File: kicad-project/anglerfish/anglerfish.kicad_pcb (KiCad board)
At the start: 2 copper layers, 276.9 x 188 mm, 4 parts

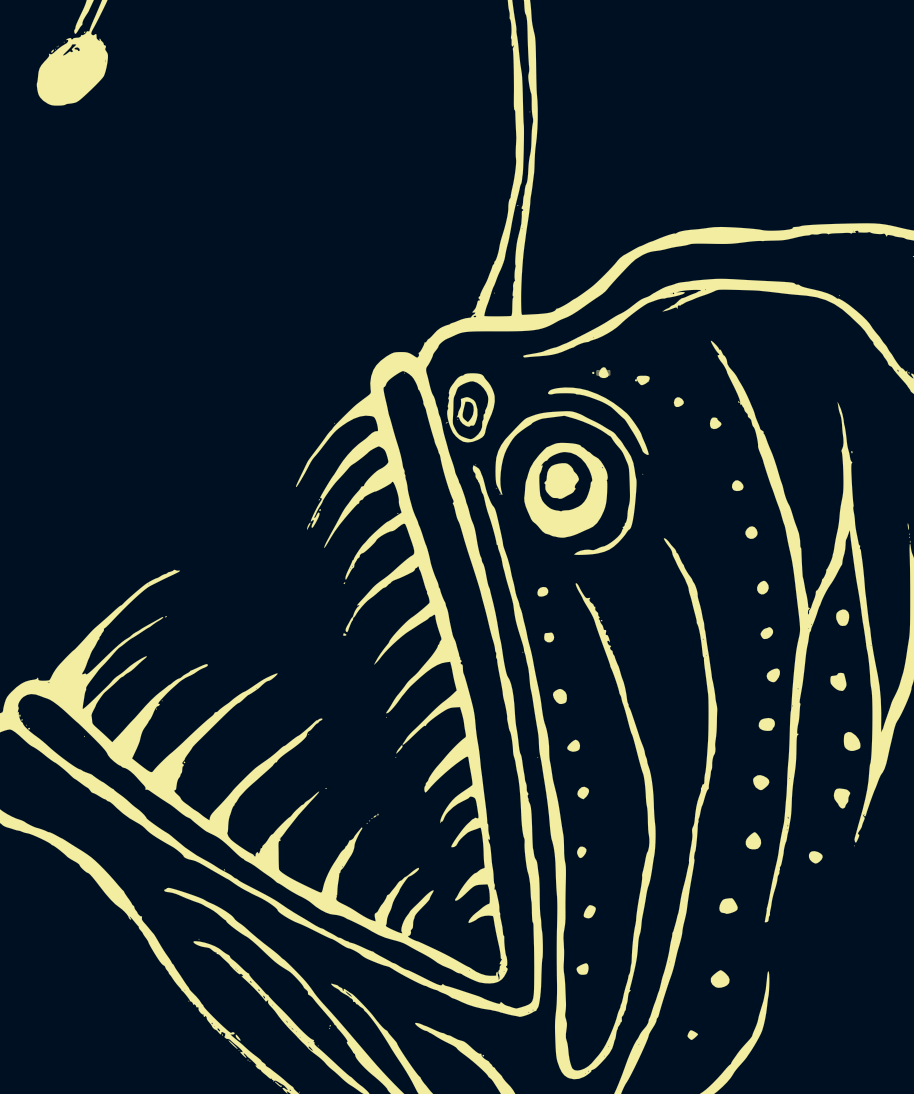
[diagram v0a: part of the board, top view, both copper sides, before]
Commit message: Added the 0402 whites. Also added the APA.
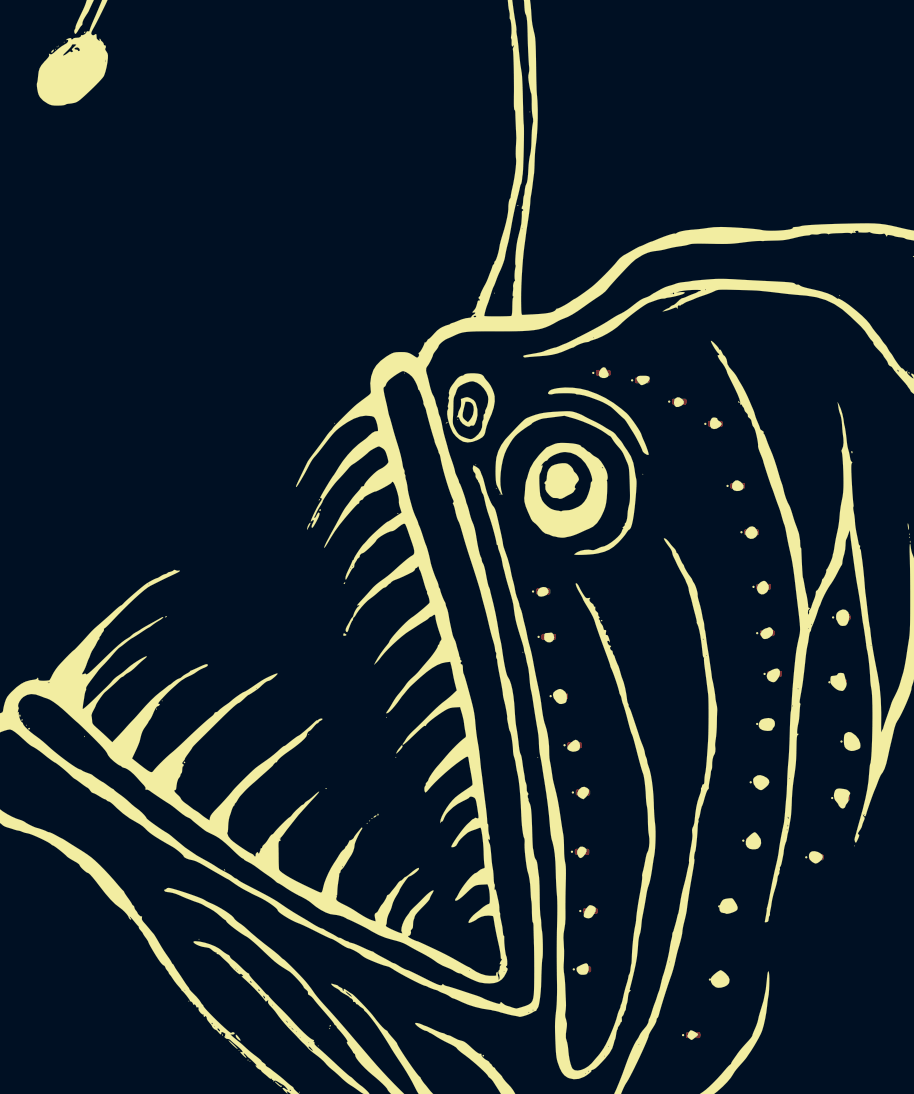
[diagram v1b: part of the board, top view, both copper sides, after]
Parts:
- added D10: LED, LED_SMD:LED_0402_1005Metric, F.Cu at (135.6, 120.1)
- added D11: LED, LED_SMD:LED_0402_1005Metric, F.Cu at (134.8, 125.5)
- added D12: LED, LED_SMD:LED_0402_1005Metric, F.Cu at (134.1, 131.8)
- added D13: LED, LED_SMD:LED_0402_1005Metric, F.Cu at (133.3, 138.1)
- added D14: LED, LED_SMD:LED_0402_1005Metric, F.Cu at (130.7, 145.2)
- added D15: LED, LED_SMD:LED_0402_1005Metric, F.Cu at (129.7, 153.1)
- added D16: LED, LED_SMD:LED_0402_1005Metric, F.Cu at (126.8, 159.1)
- added D17: LED, LED_SMD:LED_0402_1005Metric, F.Cu at (115.0, 152.0)
- added D18: LED, LED_SMD:LED_0402_1005Metric, F.Cu at (115.7, 145.7)
- added D19: LED, LED_SMD:LED_0402_1005Metric, F.Cu at (114.8, 139.3)
- added D20: LED, LED_SMD:LED_0402_1005Metric, F.Cu at (114.9, 132.9)
- added D21: LED, LED_SMD:LED_0402_1005Metric, F.Cu at (114.0, 127.8)
- added D22: LED, LED_SMD:LED_0402_1005Metric, F.Cu at (112.5, 122.5)
- added D23: LED, LED_SMD:LED_0402_1005Metric, F.Cu at (111.2, 116.1)
- added D24: LED, LED_SMD:LED_0402_1005Metric, F.Cu at (110.6, 111.2)
- added D25: LED, LED_SMD:LED_0402_1005Metric, F.Cu at (143.0, 114.0)
- added D26: LED, LED_SMD:LED_0402_1005Metric, F.Cu at (142.6, 121.0)
- added D27: LED, LED_SMD:LED_0402_1005Metric, F.Cu at (143.9, 127.4)
- added D28: LED, LED_SMD:LED_0402_1005Metric, F.Cu at (142.9, 133.5)
- added D29: LED, LED_SMD:LED_0402_1005Metric, F.Cu at (140.1, 139.9)
- added D4: LED, LED_SMD:LED_0402_1005Metric, F.Cu at (125.3, 90.7)
- added D5: LED, LED_SMD:LED_0402_1005Metric, F.Cu at (129.2, 93.1)
- added D6: LED, LED_SMD:LED_0402_1005Metric, F.Cu at (131.6, 99.8)
- added D7: LED, LED_SMD:LED_0402_1005Metric, F.Cu at (133.1, 104.8)
- added D8: LED, LED_SMD:LED_0402_1005Metric, F.Cu at (134.4, 110.7)
- added D9: LED, LED_SMD:LED_0402_1005Metric, F.Cu at (134.8, 115.7)
- D1: value LED -> APA102-2020; footprint LED_SMD:LED_0603_1608Metric -> LED_SMD:LED-APA102-2020
- D3: footprint LED_SMD:LED_0201_0603Metric -> LED_SMD:LED_0402_1005Metric
- moved D1 0.67 mm to (59.8, 55.2)
- moved D3 0.20 mm to (121.3, 88.4)

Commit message: Added the photodiode.
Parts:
- added C1: 100n, Capacitor_SMD:C_0402_1005Metric, B.Cu at (106.2, 91.6)
- added D30: LED, LED_SMD:LED_0402_1005Metric, F.Cu at (112.5, 99.3)
- added TP1: TestPoint, TestPoint:TestPoint_Pad_D1.5mm, B.Cu at (99.5, 91.7)
- added TP2: TestPoint, TestPoint:TestPoint_Pad_D1.5mm, B.Cu at (101.9, 88.3)
- added TP3: TestPoint, TestPoint:TestPoint_Pad_D1.5mm, B.Cu at (105.3, 94.1)
- added U1: APDS-9306-065, OptoDevice:Broadcom_DFN-6_2x2mm_P0.65mm, F.Cu at (102.6, 91.7)

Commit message: ZIF connector added.
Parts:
- added J1: Conn_01x34_MountingPin, Connector_FFC-FPC:Hirose_FH12-34S-0.5SH_1x34-1MP_P0.50mm_Horizontal, B.Cu at (151.0, 52.0)

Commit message: Schematic entered. Adding placing the resistors in the layout now.
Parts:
- added C2: 100n, Capacitor_SMD:C_0402_1005Metric, F.Cu at (60.0, 62.0)
- added R1: R_Small_US, Resistor_SMD:R_0402_1005Metric, B.Cu at (117.1, 86.4)
- added R10: R_Small_US, Resistor_SMD:R_0402_1005Metric, F.Cu at (35.1, 85.0)
- added R11: R_Small_US, Resistor_SMD:R_0402_1005Metric, B.Cu at (134.1, 130.7)
- added R12: R_Small_US, Resistor_SMD:R_0402_1005Metric, B.Cu at (133.3, 137.0)
- added R13: R_Small_US, Resistor_SMD:R_0402_1005Metric, F.Cu at (38.6, 83.0)
- added R14: R_Small_US, Resistor_SMD:R_0402_1005Metric, F.Cu at (41.5, 81.0)
- added R15: R_Small_US, Resistor_SMD:R_0402_1005Metric, F.Cu at (35.7, 83.0)
- added R16: R_Small_US, Resistor_SMD:R_0402_1005Metric, F.Cu at (38.0, 87.0)
- added R17: R_Small_US, Resistor_SMD:R_0402_1005Metric, F.Cu at (40.9, 85.0)
- added R18: R_Small_US, Resistor_SMD:R_0402_1005Metric, B.Cu at (114.8, 138.2)
- added R19: R_Small_US, Resistor_SMD:R_0402_1005Metric, B.Cu at (114.9, 131.8)
- added R2: R_Small_US, Resistor_SMD:R_0402_1005Metric, F.Cu at (28.6, 88.1)
- added R20: R_Small_US, Resistor_SMD:R_0402_1005Metric, F.Cu at (43.8, 87.0)
- added R21: R_Small_US, Resistor_SMD:R_0402_1005Metric, B.Cu at (112.5, 121.4)
- added R22: R_Small_US, Resistor_SMD:R_0402_1005Metric, F.Cu at (43.8, 85.0)
- added R23: R_Small_US, Resistor_SMD:R_0402_1005Metric, F.Cu at (44.5, 83.0)
- added R24: R_Small_US, Resistor_SMD:R_0402_1005Metric, B.Cu at (143.0, 112.7)
- added R25: R_Small_US, Resistor_SMD:R_0402_1005Metric, F.Cu at (40.9, 87.0)
- added R26: R_Small_US, Resistor_SMD:R_0402_1005Metric, B.Cu at (143.9, 126.3)
- added R27: R_Small_US, Resistor_SMD:R_0402_1005Metric, F.Cu at (38.0, 85.0)
- added R28: R_Small_US, Resistor_SMD:R_0402_1005Metric, F.Cu at (56.0, 71.0)
- added R29: R_Small_US, Resistor_SMD:R_0402_1005Metric, F.Cu at (41.5, 83.0)
- added R3: R_Small_US, Resistor_SMD:R_0402_1005Metric, F.Cu at (32.2, 84.5)
- added R4: R_Small_US, Resistor_SMD:R_0402_1005Metric, F.Cu at (35.7, 81.0)
- added R5: R_Small_US, Resistor_SMD:R_0402_1005Metric, B.Cu at (131.6, 99.8)
- added R6: R_Small_US, Resistor_SMD:R_0402_1005Metric, B.Cu at (133.1, 103.7)
- added R7: R_Small_US, Resistor_SMD:R_0402_1005Metric, F.Cu at (32.2, 86.5)
- added R8: R_Small_US, Resistor_SMD:R_0402_1005Metric, F.Cu at (38.6, 81.0)
- added R9: R_Small_US, Resistor_SMD:R_0402_1005Metric, B.Cu at (135.6, 119.0)
- added TP4: TestPoint, TestPoint:TestPoint_Pad_D1.5mm, F.Cu at (32.5, 81.8)
- added TP5: TestPoint, TestPoint:TestPoint_Pad_D1.5mm, F.Cu at (28.9, 85.3)
- added TP6: TestPoint, TestPoint:TestPoint_Pad_D1.5mm, F.Cu at (25.4, 88.9)
- added TP7: TestPoint, TestPoint:TestPoint_Pad_D1.5mm, F.Cu at (28.9, 81.8)
- added TP8: TestPoint, TestPoint:TestPoint_Pad_D1.5mm, F.Cu at (25.4, 85.3)
- added TP9: TestPoint, TestPoint:TestPoint_Pad_D1.5mm, F.Cu at (25.4, 81.8)
- J1: value Conn_01x34_MountingPin -> Hirose_FH12-34S-0.5SH_1x34
- moved D1 0.28 mm to (60.0, 55.0)
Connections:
- net /Sheet5FEEB7DF/light-int renamed /photodiode-1/photodiode-int
- net Net-(D1-Pad2) renamed /led-apa102-1/apa102-cko
- net Net-(D1-Pad3) renamed /led-apa102-1/apa102-sdo
- D1 pad 4: Net-(D1-Pad4) -> /led-apa102-1/apa102-sdi
- D1 pad 5: Net-(D1-Pad5) -> /led-apa102-1/apa102-cki
- D1 pad 6: Net-(D1-Pad6) -> GND
- D10 pad 2: Net-(D10-Pad2) -> /LED_GROUP_2
- D11 pad 2: Net-(D11-Pad2) -> /LED_GROUP_2
- D12 pad 2: Net-(D12-Pad2) -> /LED_GROUP_3
- D13 pad 2: Net-(D13-Pad2) -> /LED_GROUP_3
- D14 pad 2: Net-(D14-Pad2) -> /LED_GROUP_3
- D15 pad 2: Net-(D15-Pad2) -> /LED_GROUP_3
- D16 pad 2: Net-(D16-Pad2) -> /LED_GROUP_3
- D17 pad 2: Net-(D17-Pad2) -> /LED_GROUP_4
- D18 pad 2: Net-(D18-Pad2) -> /LED_GROUP_4
- D19 pad 2: Net-(D19-Pad2) -> /LED_GROUP_4
- D2 pad 2: Net-(D2-Pad2) -> /LED_GROUP_1
- D20 pad 2: Net-(D20-Pad2) -> /LED_GROUP_4
- D21 pad 2: Net-(D21-Pad2) -> /LED_GROUP_4
- D22 pad 2: Net-(D22-Pad2) -> /LED_GROUP_5
- D23 pad 2: Net-(D23-Pad2) -> /LED_GROUP_5
- D24 pad 2: Net-(D24-Pad2) -> /LED_GROUP_5
- D25 pad 2: Net-(D25-Pad2) -> /LED_GROUP_5
- D26 pad 2: Net-(D26-Pad2) -> /LED_GROUP_5
- D27 pad 2: Net-(D27-Pad2) -> /LED_GROUP_6
- D28 pad 2: Net-(D28-Pad2) -> /LED_GROUP_6
- D29 pad 2: Net-(D29-Pad2) -> /LED_GROUP_6
- D3 pad 2: Net-(D3-Pad2) -> /LED_GROUP_1
- D30 pad 2: Net-(D30-Pad2) -> /LED_GROUP_6
- D4 pad 2: Net-(D4-Pad2) -> /LED_GROUP_1
- D5 pad 2: Net-(D5-Pad2) -> /LED_GROUP_1
- D6 pad 2: Net-(D6-Pad2) -> /LED_GROUP_1
- D7 pad 2: Net-(D7-Pad2) -> /LED_GROUP_2
- D8 pad 2: Net-(D8-Pad2) -> /LED_GROUP_2
- D9 pad 2: Net-(D9-Pad2) -> /LED_GROUP_2
- J1 pad 1: Net-(J1-Pad1) -> +3V3
- J1 pad 11: Net-(J1-Pad11) -> /led-apa102-1/apa102-sdi
- J1 pad 12: Net-(J1-Pad12) -> /led-apa102-1/apa102-cki
- J1 pad 14: Net-(J1-Pad14) -> GND
- J1 pad 15: Net-(J1-Pad15) -> /LED_GROUP_1
- J1 pad 16: Net-(J1-Pad16) -> /LED_GROUP_2
- J1 pad 17: Net-(J1-Pad17) -> /LED_GROUP_3
- J1 pad 18: Net-(J1-Pad18) -> /LED_GROUP_4
- J1 pad 19: Net-(J1-Pad19) -> /LED_GROUP_5
- J1 pad 2: Net-(J1-Pad2) -> +3V3
- J1 pad 20: Net-(J1-Pad20) -> /LED_GROUP_6
- J1 pad 3: Net-(J1-Pad3) -> +5V
- J1 pad 4: Net-(J1-Pad4) -> +5V
- J1 pad 5: Net-(J1-Pad5) -> GND
- J1 pad 6: Net-(J1-Pad6) -> GND
- J1 pad 7: Net-(J1-Pad7) -> /photodiode-scl
- J1 pad 8: Net-(J1-Pad8) -> /photodiode-sda
- J1 pad 9: Net-(J1-Pad9) -> GND
- J1 pad MP: Net-(J1-PadMP) -> GND
- TP1 pad 1: /Sheet5FEEB7DF/light-sda -> /photodiode-sda
- TP2 pad 1: /Sheet5FEEB7DF/light-scl -> /photodiode-scl
- U1 pad 1: /Sheet5FEEB7DF/light-scl -> /photodiode-scl
- U1 pad 2: /Sheet5FEEB7DF/light-sda -> /photodiode-sda
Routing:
- net Net-(D25-Pad1): track 0.00 -> 3.37 mm, vias 0 -> 1
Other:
- net class Default: via_dia 0.8 -> 0.6; via_drill 0.4 -> 0.3
- rule via_min_drill: 0.3 -> 0.2
- rule via_min_size: 0.4 -> 0.6

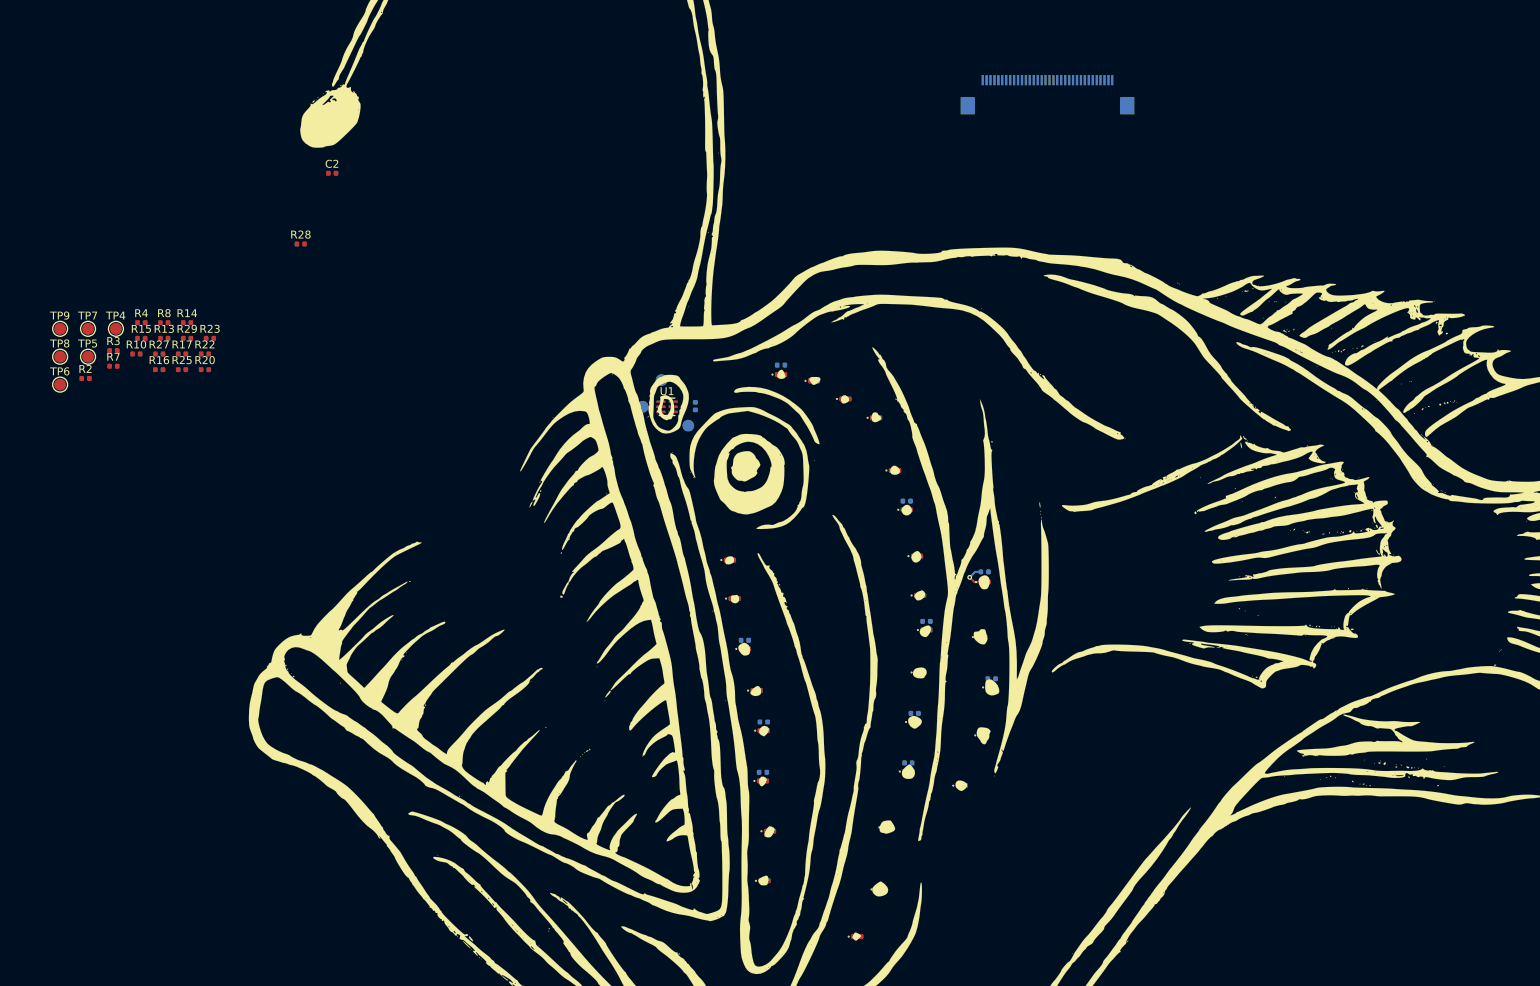
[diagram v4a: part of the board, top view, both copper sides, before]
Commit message: Did placement. Need to edit the silkscreen layer to carve out an opening for the neo LED.
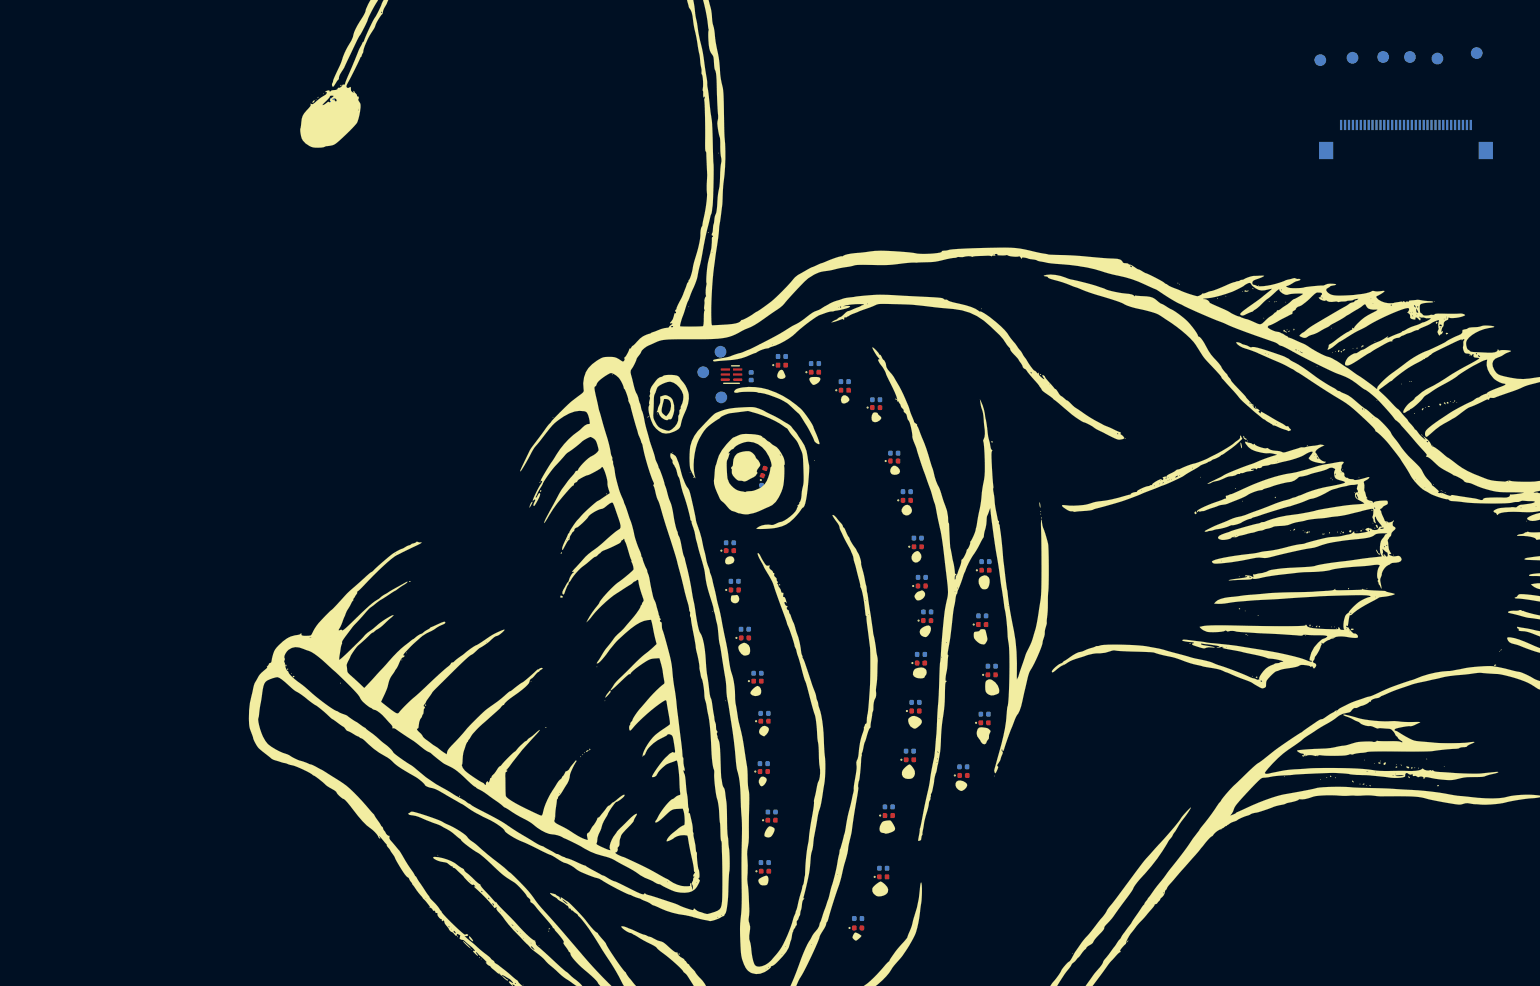
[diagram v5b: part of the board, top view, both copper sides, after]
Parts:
- C2, R10, R13, R14, R15, R16, R17, R2, R20, R22, R23, R25, R27, R28, R29, R3, R4, R7, R8, TP4, TP5, TP6, TP7, TP8, TP9: moved to B.Cu
- moved TP5 180.8 mm to (205.6, 46.7)
- moved TP6 176.7 mm to (197.1, 47.2)
- moved TP4 171.6 mm to (200.6, 47.4)
- moved TP8 168.8 mm to (189.8, 47.3)
- moved TP7 168.3 mm to (193.7, 47.2)
- moved TP9 163.9 mm to (185.7, 47.6)
- moved R15 117.3 mm to (126.9, 156.8)
- moved R27 114.6 mm to (143.0, 130.8)
- moved R14 112.5 mm to (130.1, 150.4)
- moved R13 109.8 mm to (130.8, 142.6)
- moved R28 107.4 mm to (140.3, 137.5)
- moved R10 106.9 mm to (134.9, 123.2)
- moved R25 106.5 mm to (142.7, 118.3)
- moved R7 104.6 mm to (134.5, 108.4)
- moved R8 101.7 mm to (135.0, 113.4)
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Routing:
- net Net-(D25-Pad1): track 3.37 -> 0.00 mm, vias 1 -> 0

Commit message: Routed the LED's and their resistors. Placed comments on the areas where the artwork needs rework.
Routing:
- net /LED_GROUP_3: track 0.00 -> 36.5 mm, vias 0 -> 5
- net /LED_GROUP_1: track 0.00 -> 32.4 mm, vias 0 -> 5
- net /LED_GROUP_4: track 0.00 -> 30.7 mm, vias 0 -> 5
- net GND: track 0.00 -> 7.82 mm, vias 0 -> 1
- net +3V3: track 0.00 -> 6.81 mm, vias 0 -> 1
- net Net-(D30-Pad1): track 0.00 -> 3.15 mm, vias 0 -> 1
- net /photodiode-1/photodiode-int: track 0.00 -> 3.11 mm, vias 0 -> 1
- net Net-(D28-Pad1): track 0.00 -> 3.09 mm, vias 0 -> 1
- net /photodiode-sda: track 0.00 -> 2.94 mm, vias 0 -> 1
- net Net-(D23-Pad1): track 0.00 -> 2.90 mm, vias 0 -> 1
- net Net-(D22-Pad1): track 0.00 -> 2.90 mm, vias 0 -> 1
- net Net-(D27-Pad1): track 0.00 -> 2.89 mm, vias 0 -> 1
- net Net-(D11-Pad1): track 0.00 -> 2.89 mm, vias 0 -> 1
- net Net-(D8-Pad1): track 0.00 -> 2.87 mm, vias 0 -> 1
- net Net-(D24-Pad1): track 0.00 -> 2.84 mm, vias 0 -> 1
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- added copper zone on B.Cu, net GND
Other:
- board text added: "need to create a hole in fish's light to fit the digi led."
- board text added: "these parts will look ugly. clean up."

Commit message: Finished routing. trying to generate a bom.
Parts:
- moved TP4 1.46 mm to (202.0, 47.0)
- moved TP6 0.92 mm to (198.0, 47.0)
- moved TP9 0.67 mm to (186.0, 47.0)
- moved TP5 0.50 mm to (206.0, 47.0)
- moved TP7 0.36 mm to (194.0, 47.0)
- moved TP8 0.30 mm to (189.8, 47.0)
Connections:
- J1 pad 11: /led-apa102-1/apa102-sdi -> /led-apa102-1/apa102-cki
- J1 pad 12: /led-apa102-1/apa102-cki -> /led-apa102-1/apa102-sdi
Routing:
- net /LED_GROUP_5: track 0.00 -> 266.0 mm, vias 0 -> 5
- net /LED_GROUP_6: track 0.00 -> 194.0 mm, vias 0 -> 6
- net /led-apa102-1/apa102-cki: track 0.00 -> 182.9 mm, vias 0 -> 1
- net /led-apa102-1/apa102-sdi: track 0.00 -> 182.2 mm, vias 0 -> 1
- net /LED_GROUP_4: track 30.7 -> 201.6 mm, vias 5 -> 7
- net /LED_GROUP_1: track 32.4 -> 180.6 mm
- net /LED_GROUP_3: track 36.5 -> 172.0 mm, vias 5 -> 7
- net /LED_GROUP_2: track 0.00 -> 129.3 mm, vias 0 -> 8
- net /photodiode-sda: track 2.94 -> 115.0 mm
- net +3V3: track 6.81 -> 114.9 mm
- net /photodiode-scl: track 2.50 -> 109.9 mm
- net GND: track 7.82 -> 25.1 mm, vias 1 -> 9
- net Net-(C2-Pad1): track 0.00 -> 4.89 mm, vias 0 -> 1
- added copper zone on F.Cu, net GND
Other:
- rule pad_to_mask_clearance: 0.051 -> 0
